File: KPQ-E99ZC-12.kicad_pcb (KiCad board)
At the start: 2 copper layers, 79.2 x 53 mm, 25 parts, among them J1 USB Cable, J2 Chassis, J3 SWD, J4 Edge Connector, J5 Alternate Connector 1, J6 Alternate Connector 2, SW1 BOOT, U1 USBLC6-2SC6, U2 XC6206P332MR-G, U3 STM32C071KBT6

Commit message: Update net classes
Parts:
- moved R2 11.4 mm to (96.9, 50.8), turned to 180 degrees
- moved R1 5.88 mm to (83.1, 60.7)
- moved SD1 3.62 mm to (88.4, 69.2)
- moved SW1 3.59 mm to (81.4, 65.4)
- moved F1 1.38 mm to (88.6, 71.2)
- moved C8 0.88 mm to (51.5, 47.8), turned to 180 degrees
- moved C6 0.88 mm to (93.8, 47.8), turned to 180 degrees
- moved C7 0.88 mm to (72.7, 47.8), turned to 180 degrees
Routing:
- net Col16: track 9.93 -> 62.2 mm
- net Col15: track 9.70 -> 59.5 mm
- net Col14: track 9.48 -> 56.6 mm
- net Col13: track 9.26 -> 53.9 mm
- net Row1: track 9.93 -> 53.8 mm
- net Col12: track 9.03 -> 50.3 mm
- net Row2: track 9.70 -> 50.7 mm
- net Row3: track 9.48 -> 47.5 mm
- net Col11: track 8.81 -> 46.7 mm
- net Col10: track 8.59 -> 45.3 mm
- net Row4: track 9.26 -> 45.5 mm
- net SWDIO: track 0.00 -> 34.9 mm
- net Row5: track 9.03 -> 43.6 mm
- net NRST: track 3.03 -> 37.5 mm, vias 0 -> 1
- net Col9: track 8.36 -> 42.5 mm
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
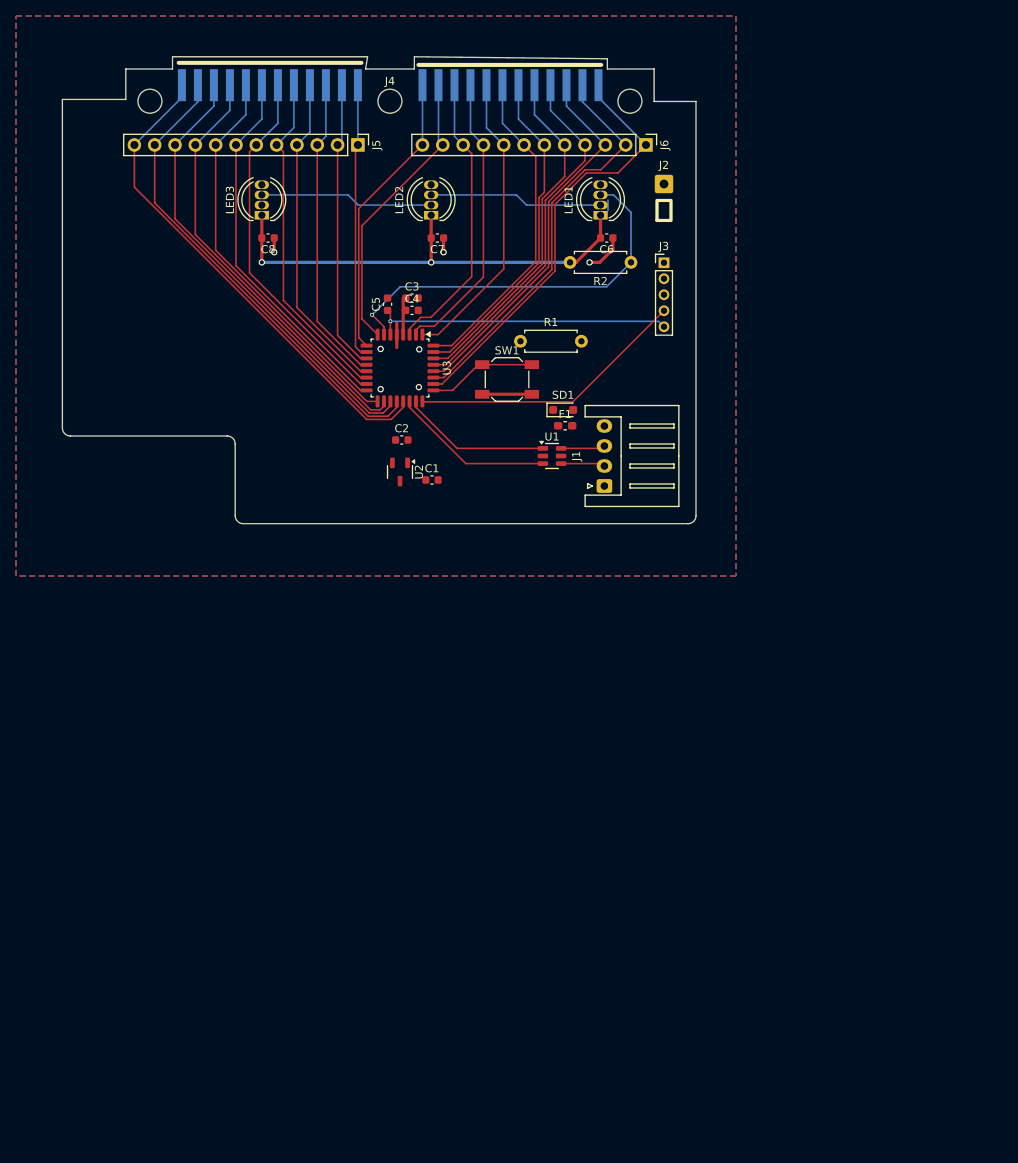
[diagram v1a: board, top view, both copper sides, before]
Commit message: Add measurements and tweak positions
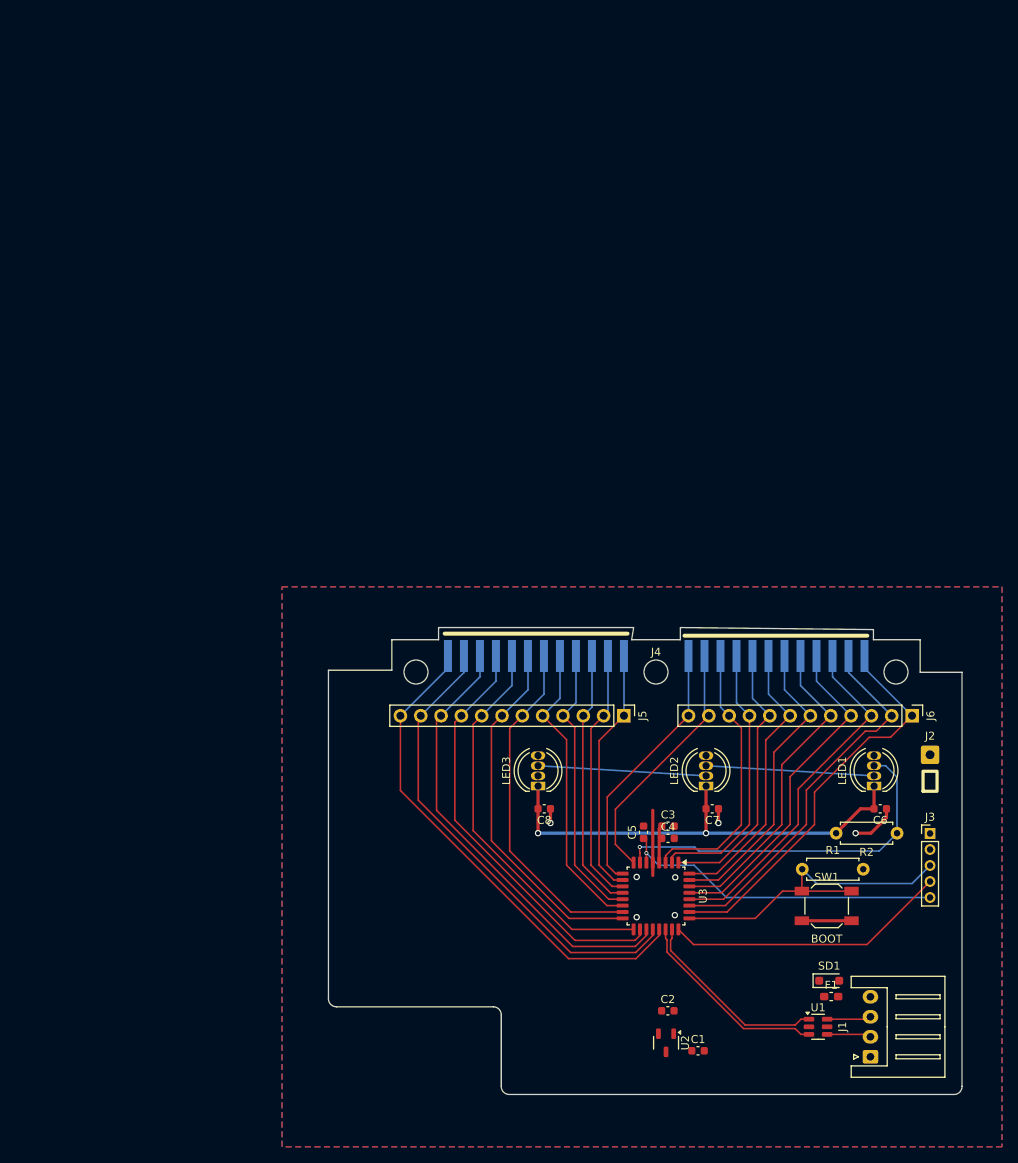
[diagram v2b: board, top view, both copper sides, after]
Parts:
- moved C8 79.3 mm to (86.0, 119.1)
- moved LED3 79.3 mm to (85.3, 116.3)
- moved C7 79.2 mm to (107.0, 119.1)
- moved LED2 79.2 mm to (106.3, 116.3)
- moved C6 79.1 mm to (128.0, 119.1)
- moved LED1 79.1 mm to (127.3, 116.3)
- moved C1 78.7 mm to (105.3, 149.3)
- moved C2 78.7 mm to (101.5, 144.3)
- moved F1 78.7 mm to (121.9, 142.6)
- moved J1 78.7 mm to (126.8, 150.1)
- moved J2 78.7 mm to (134.3, 112.3)
- moved J3 78.7 mm to (134.3, 122.2)
- moved J4 78.7 mm to (100.0, 100.0)
- moved J5 78.7 mm to (96.0, 107.5)
- moved J6 78.7 mm to (132.0, 107.5)
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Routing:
- net BOOT0/SWCLK: track 13.6 -> 42.1 mm
- net GND: track 11.6 -> 17.5 mm
- net Col7: track 38.4 -> 32.9 mm
- net USB_D+: track 18.7 -> 24.2 mm
- net Row7: track 40.9 -> 35.5 mm
- net Col8: track 40.5 -> 35.2 mm
- net Col9: track 42.5 -> 37.4 mm
- net Row1: track 53.8 -> 48.8 mm
- net LED: track 50.4 -> 45.7 mm
- net USB_D-: track 20.3 -> 24.9 mm
- net Col3: track 36.4 -> 31.8 mm
- net Col6: track 36.3 -> 32.1 mm
- net Row6: track 41.6 -> 37.7 mm
- net Row5: track 43.6 -> 39.9 mm
- net Col4: track 36.3 -> 32.7 mm
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
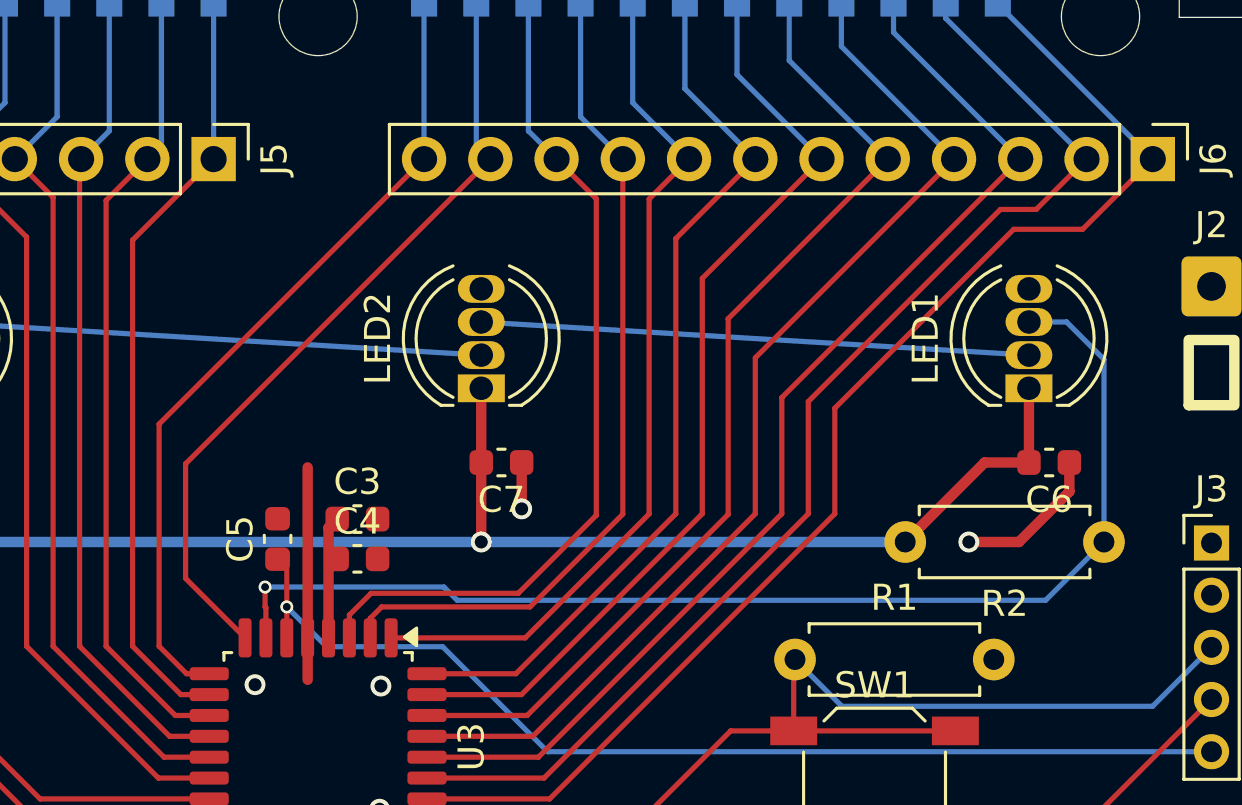
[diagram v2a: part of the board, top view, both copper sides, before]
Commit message: Swap LED pin
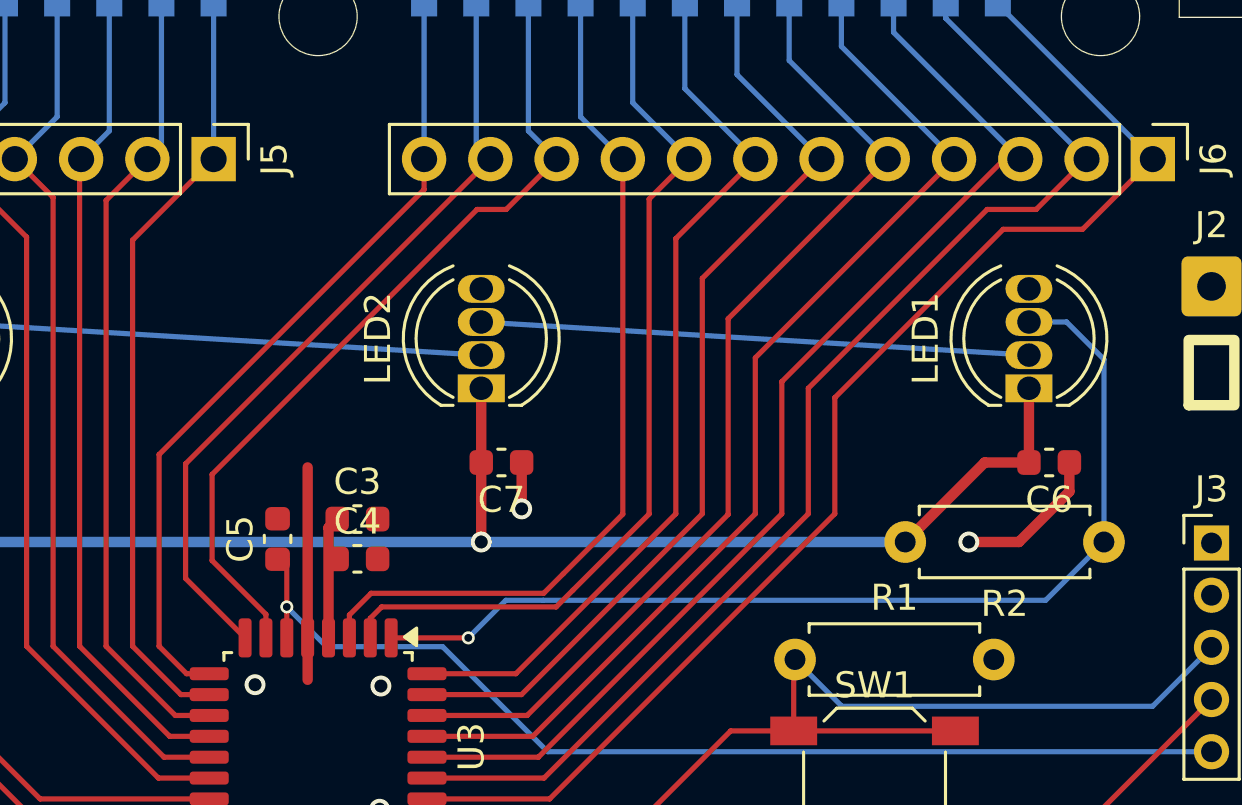
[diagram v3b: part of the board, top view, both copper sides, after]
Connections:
- U3 pad 1: Row8 -> LED
- U3 pad 2: Col1 -> Row8
- U3 pad 3: Col2 -> Col1
- U3 pad 7: LED -> Col2
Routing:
- net LED: track 45.7 -> 39.3 mm
- net Row8: track 34.5 -> 35.7 mm
- net Col2: track 34.1 -> 33.3 mm
- net Col1: track 33.8 -> 34.7 mm
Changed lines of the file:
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@@
 			(layers "F.Cu" "F.Mask" "F.Paste")
 			(roundrect_rratio 0.25)
-			(net 32 "Row8")
+			(net 34 "LED")
 			(pinfunction "PB9")
 			(pintype "bidirectional")
@@
 			(layers "F.Cu" "F.Mask" "F.Paste")
 			(roundrect_rratio 0.25)
-			(net 23 "Col1")
+			(net 32 "Row8")
 			(pinfunction "PC14")
 			(pintype "bidirectional")
@@
 			(layers "F.Cu" "F.Mask" "F.Paste")
 			(roundrect_rratio 0.25)
-			(net 25 "Col2")
+			(net 23 "Col1")
 			(pinfunction "PC15")
 			(pintype "bidirectional")
@@
 			(layers "F.Cu" "F.Mask" "F.Paste")
 			(roundrect_rratio 0.25)
-			(net 34 "LED")
+			(net 25 "Col2")
 			(pinfunction "PA0")
 			(pintype "bidirectional")
@@
 	)
 	(segment
-		(start 126.67 110.16)
-		(end 119.812 117.018)
+		(start 132.004 107.4676)
+		(end 129.3116 110.16)
 		(width 0.2)
 		(layer "F.Cu")
@@
 	)
 	(segment
-		(start 119.812 121.0672)
-		(end 119.812 117.018)
+		(start 108.8792 132)
+		(end 104.175 132)
 		(width 0.2)
 		(layer "F.Cu")
@@
 	)
 	(segment
-		(start 129.3116 110.16)
-		(end 126.67 110.16)
+		(start 126.267942 110.16)
+		(end 119.812 116.615942)
 		(width 0.2)
 		(layer "F.Cu")
@@
 	)
 	(segment
-		(start 108.8792 132)
-		(end 104.175 132)
+		(start 129.3116 110.16)
+		(end 126.267942 110.16)
 		(width 0.2)
 		(layer "F.Cu")
@@
 	)
 	(segment
-		(start 132.004 107.4676)
-		(end 129.3116 110.16)
+		(start 119.812 116.615942)
+		(end 119.812 121.0672)
 		(width 0.2)
 		(layer "F.Cu")
@@
 	)
 	(segment
-		(start 102 125.075001)
-		(end 102.437001 124.638)
+		(start 111.684 121.082)
+		(end 111.684 107.4676)
 		(width 0.2)
 		(layer "F.Cu")
@@
 	)
 	(segment
-		(start 102.437001 124.638)
-		(end 108.128 124.638)
+		(start 101.2 125.825)
+		(end 101.2 124.9472)
 		(width 0.2)
 		(layer "F.Cu")
@@
 	)
 	(segment
-		(start 102 125.825)
-		(end 102 125.075001)
+		(start 102.032 124.1152)
+		(end 108.6508 124.1152)
 		(width 0.2)
 		(layer "F.Cu")
@@
 	)
 	(segment
-		(start 111.684 121.082)
-		(end 111.684 107.4676)
+		(start 108.6508 124.1152)
+		(end 109.398 123.368)
 		(width 0.2)
 		(layer "F.Cu")
@@
 	)
 	(segment
-		(start 108.128 124.638)
+		(start 109.398 123.368)
 		(end 111.684 121.082)
 		(width 0.2)
@@
 	)
 	(segment
+		(start 101.2 124.9472)
+		(end 102.032 124.1152)
+		(width 0.2)
+		(layer "F.Cu")
+		(net 23)
+	)
+	(segment
 		(start 110.064 100)
 		(end 110.064 105.8476)
@@
 	)
 	(segment
-		(start 94.92 119.1516)
-		(end 106.604 107.4676)
+		(start 97.2 125.825)
+		(end 94.92 123.545)
 		(width 0.2)
 		(layer "F.Cu")
@@
 	)
 	(segment
-		(start 97.2 125.825)
-		(end 94.92 123.545)
+		(start 94.92 119.1516)
+		(end 106.604 107.4676)
 		(width 0.2)
 		(layer "F.Cu")
@@
 	)
 	(segment
-		(start 102.032 124.1152)
-		(end 107.676745 124.1152)
+		(start 98 125.825)
+		(end 98 124.924)
 		(width 0.2)
 		(layer "F.Cu")
@@
 	)
 	(segment
-		(start 110.668 121.123945)
-		(end 110.668 108.9916)
+		(start 107.2136 109.398)
+		(end 109.144 107.4676)
 		(width 0.2)
 		(layer "F.Cu")
@@
 	)
 	(segment
-		(start 101.2 125.825)
-		(end 101.2 124.9472)
+		(start 106.096 109.398)
+		(end 107.2136 109.398)
 		(width 0.2)
 		(layer "F.Cu")
@@
 	)
 	(segment
-		(start 110.668 108.9916)
-		(end 109.144 107.4676)
+		(start 98 124.924)
+		(end 95.936 122.86)
 		(width 0.2)
 		(layer "F.Cu")
@@
 	)
 	(segment
-		(start 107.676745 124.1152)
-		(end 110.668 121.123945)
+		(start 95.936 119.558)
+		(end 106.096 109.398)
 		(width 0.2)
 		(layer "F.Cu")
@@
 	)
 	(segment
-		(start 101.2 124.9472)
-		(end 102.032 124.1152)
+		(start 95.936 122.86)
+		(end 95.936 119.558)
 		(width 0.2)
 		(layer "F.Cu")
@@
 	)
 	(segment
-		(start 118.796 121.0672)
-		(end 108.6632 131.2)
+		(start 118.796 116.256)
+		(end 118.796 121.0672)
 		(width 0.2)
 		(layer "F.Cu")
@@
 	)
 	(segment
-		(start 126.162 109.398)
-		(end 118.796 116.764)
+		(start 125.654 109.398)
+		(end 118.796 116.256)
 		(width 0.2)
 		(layer "F.Cu")
@@
 	)
 	(segment
-		(start 129.464 107.4676)
-		(end 127.5336 109.398)
+		(start 108.6632 131.2)
+		(end 104.175 131.2)
 		(width 0.2)
 		(layer "F.Cu")
@@
 	)
 	(segment
-		(start 108.6632 131.2)
-		(end 104.175 131.2)
+		(start 118.796 121.0672)
+		(end 108.6632 131.2)
 		(width 0.2)
 		(layer "F.Cu")
@@
 	)
 	(segment
-		(start 118.796 121.0672)
-		(end 118.796 116.764)
+		(start 129.464 107.4676)
+		(end 127.5336 109.398)
 		(width 0.2)
 		(layer "F.Cu")
@@
 	(segment
 		(start 127.5336 109.398)
-		(end 126.162 109.398)
+		(end 125.654 109.398)
 		(width 0.2)
 		(layer "F.Cu")
@@
 	)
 	(segment
-		(start 108.4472 130.4)
-		(end 117.78 121.0672)
+		(start 117.78 121.0672)
+		(end 117.78 116.002)
 		(width 0.2)
 		(layer "F.Cu")
@@
 	)
 	(segment
-		(start 117.78 116.6116)
-		(end 126.924 107.4676)
+		(start 108.4472 130.4)
+		(end 117.78 121.0672)
 		(width 0.2)
 		(layer "F.Cu")
@@
 	)
 	(segment
-		(start 117.78 121.0672)
-		(end 117.78 116.6116)
+		(start 126.3144 107.4676)
+		(end 126.924 107.4676)
+		(width 0.2)
+		(layer "F.Cu")
+		(net 29)
+	)
+	(segment
+		(start 117.78 116.002)
+		(end 126.3144 107.4676)
 		(width 0.2)
 		(layer "F.Cu")
@@
 	)
 	(segment
-		(start 93.904 126.1472)
-		(end 93.904 117.6276)
+		(start 93.904 118.796)
+		(end 104.064 108.636)
 		(width 0.2)
 		(layer "F.Cu")
@@
 	)
 	(segment
-		(start 93.904 117.6276)
+		(start 95.825 127.2)
+		(end 94.9568 127.2)
+		(width 0.2)
+		(layer "F.Cu")
+		(net 30)
+	)
+	(segment
+		(start 104.064 108.636)
 		(end 104.064 107.4676)
 		(width 0.2)
@@
 	)
 	(segment
-		(start 95.825 127.2)
-		(end 94.9568 127.2)
+		(start 93.904 126.1472)
+		(end 93.904 118.796)
 		(width 0.2)
 		(layer "F.Cu")
@@
 	)
 	(segment
+		(start 102 125.075001)
+		(end 102.437001 124.638)
+		(width 0.2)
+		(layer "F.Cu")
+		(net 32)
+	)
+	(segment
 		(start 112.6926 108.999)
 		(end 114.224 107.4676)
@@
 	)
 	(segment
+		(start 102.437001 124.638)
+		(end 109.1292 124.638)
+		(width 0.2)
+		(layer "F.Cu")
+		(net 32)
+	)
+	(segment
 		(start 112.6926 121.0746)
 		(end 112.6926 108.999)
@@
 	)
 	(segment
-		(start 107.9422 125.825)
-		(end 112.6926 121.0746)
+		(start 109.1292 124.638)
+		(end 109.7716 123.9956)
+		(width 0.2)
+		(layer "F.Cu")
+		(net 32)
+	)
+	(segment
+		(start 102 125.825)
+		(end 102 125.075001)
 		(width 0.2)
 		(layer "F.Cu")
@@
 	)
 	(segment
-		(start 102.8 125.825)
-		(end 107.9422 125.825)
+		(start 109.7716 123.9956)
+		(end 112.6926 121.0746)
 		(width 0.2)
 		(layer "F.Cu")
@@
 	)
 	(segment
-		(start 97.968 123.876)
-		(end 97.968 124.638)
-		(width 0.2)
-		(layer "F.Cu")
-		(net 34)
-	)
-	(segment
-		(start 97.968 124.638)
-		(end 98 124.67)
-		(width 0.2)
-		(layer "F.Cu")
-		(net 34)
-	)
-	(segment
-		(start 98 124.67)
-		(end 98 125.825)
+		(start 105.759 125.825)
+		(end 102.8 125.825)
 		(width 0.2)
 		(layer "F.Cu")
@@
 	)
 	(via
-		(at 97.968 123.876)
+		(at 105.759 125.825)
 		(size 0.5)
 		(drill 0.3)
@@
 	)
 	(segment
-		(start 130.1316 122.1488)
-		(end 130.1316 115.1456)
+		(start 107.2 124.384)
+		(end 108.636 124.384)
 		(width 0.2)
 		(layer "B.Cu")
@@
 	)
 	(segment
-		(start 104.826 123.876)
-		(end 105.334 124.384)
+		(start 130.1316 122.1488)
+		(end 130.1316 115.1456)
 		(width 0.2)
 		(layer "B.Cu")
@@
 	)
 	(segment
-		(start 105.334 124.384)
+		(start 108.636 124.384)
 		(end 127.8964 124.384)
 		(width 0.2)
@@
 	)
 	(segment
-		(start 97.968 123.876)
-		(end 104.826 123.876)
+		(start 130.1316 115.1456)
+		(end 128.6998 113.7138)
 		(width 0.2)
 		(layer "B.Cu")
@@
 	)
 	(segment
-		(start 130.1316 115.1456)
-		(end 128.6998 113.7138)
+		(start 105.759 125.825)
+		(end 107.2 124.384)
 		(width 0.2)
 		(layer "B.Cu")
